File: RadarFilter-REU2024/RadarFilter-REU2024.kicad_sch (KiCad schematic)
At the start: 41 parts, among them J1 Conn_02x15_Odd_Even, J2 Conn_01x04_Pin, J5 Conn_01x04_Pin, J6 Conn_Coaxial, J7 Conn_Coaxial, J8 Conn_Coaxial, J9 Conn_Coaxial, U2 ADA4807-2ARM

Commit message: schematic iteration 1 complete, some project-specific symbols included
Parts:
- removed C6: 0.1uF, Capacitor_SMD:C_0805_2012Metric_Pad1.18x1.45mm_HandSolder, symbol Device:C
- removed J1: Conn_02x15_Odd_Even, Connector_PinSocket_2.54mm:PinSocket_2x15_P2.54mm_Vertical, symbol Connector_Generic:Conn_02x15_Odd_Even
- removed J2 (x2), J5: Conn_01x04_Pin, Connector_PinHeader_2.54mm:PinHeader_1x04_P2.54mm_Horizontal, symbol Connector:Conn_01x04_Pin
- removed J6, J7, J8, J9: Conn_Coaxial, symbol Connector:Conn_Coaxial
- removed R10 (x4), R11 (x4): 10k, Resistor_SMD:R_0805_2012Metric_Pad1.20x1.40mm_HandSolder, symbol Device:R
- removed U2 (x4): ADA4807-2ARM, Package_SO:MSOP-8_3x3mm_P0.65mm, symbol Amplifier_Operational:ADA4807-2ARM
- added C5, C6 (x4): 0.1uF, Capacitor_SMD:C_0805_2012Metric_Pad1.18x1.45mm_HandSolder, symbol Device:C
- added C7: 10uF, Capacitor_SMD:C_0805_2012Metric_Pad1.18x1.45mm_HandSolder, symbol Device:C
- added J1, J2, J3: 73099-0, CONN_73099-0_POM, symbol 73099-0:73099-0
- added U1, U3, U4: 5227161-1, 5227161-1_TYC, symbol 5227161-1:5227161-1
- added U2: ADA4807-2ARM, Package_SO:MSOP-8_3x3mm_P0.65mm, symbol Amplifier_Operational:ADA4807-2ARM
- added unit 1 of U2
- C7: value 0.1uF -> 10uF
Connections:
- net GND: now also C5.2, C6.2, C6.2, C6.2, C6.2, C7.2, J3.1, U1.2, U2.2, U3.2, U4.2
- net V+: now also C6.1, C6.1, J2.1, U2.8 (V+)
- net V-: now also C5.1, C6.1, C6.1, C7.1, J1.1, U2.4 (V-)
- net BNC1I: now reaches R11.2, U2.7
- net BNC1I: now also U1.1
- net BNC2I: now reaches R11.2, U2.7
- net BNC2I: now also U2.1
- net 2+ renamed BNC2Q
- net BNC2Q: now also U4.1
- net BNC2 renamed BNC1Q
- net BNC1Q: now also U3.1
- no-connect marks 18 -> 0
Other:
- note added: "ADP3450 Connection - BNC Female Ports"
- note added: "Power Supply (DPS3340) - Banana Plugs"
- note added: "Trigger"
- note added: "V+/V- Bypass Capacitors"
- note removed: "AD connect"
- note removed: "Channel 3I"
- note removed: "Channel 3Q"
- note removed: "Channel 4I"
- note removed: "Channel 4Q"
- note removed: "Radar 3 Signals"
- note removed: "Radar 4 Signals"
- moved on the sheet: C5, C7, R10, R11, U2B, U2C

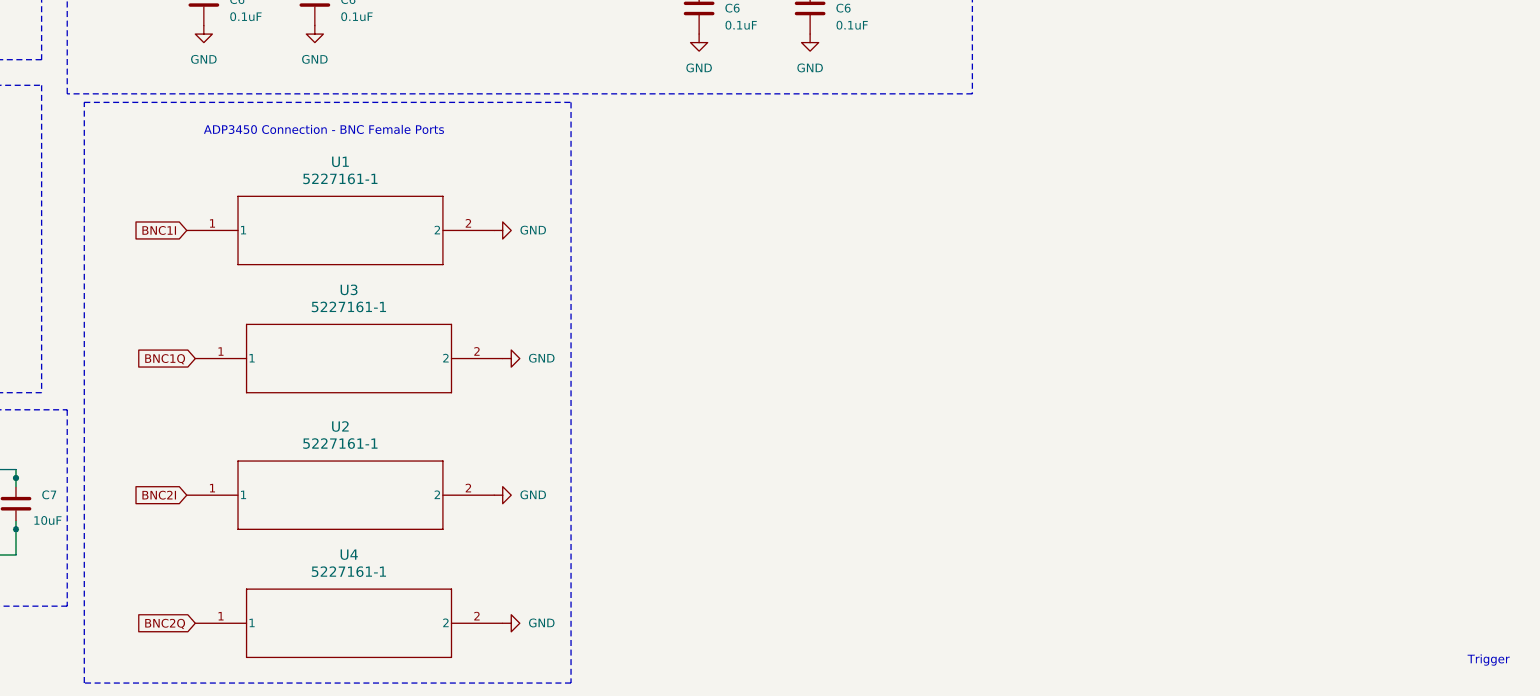
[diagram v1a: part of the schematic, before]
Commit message: changed bnc to sma connectors, attempted start at pcb layout
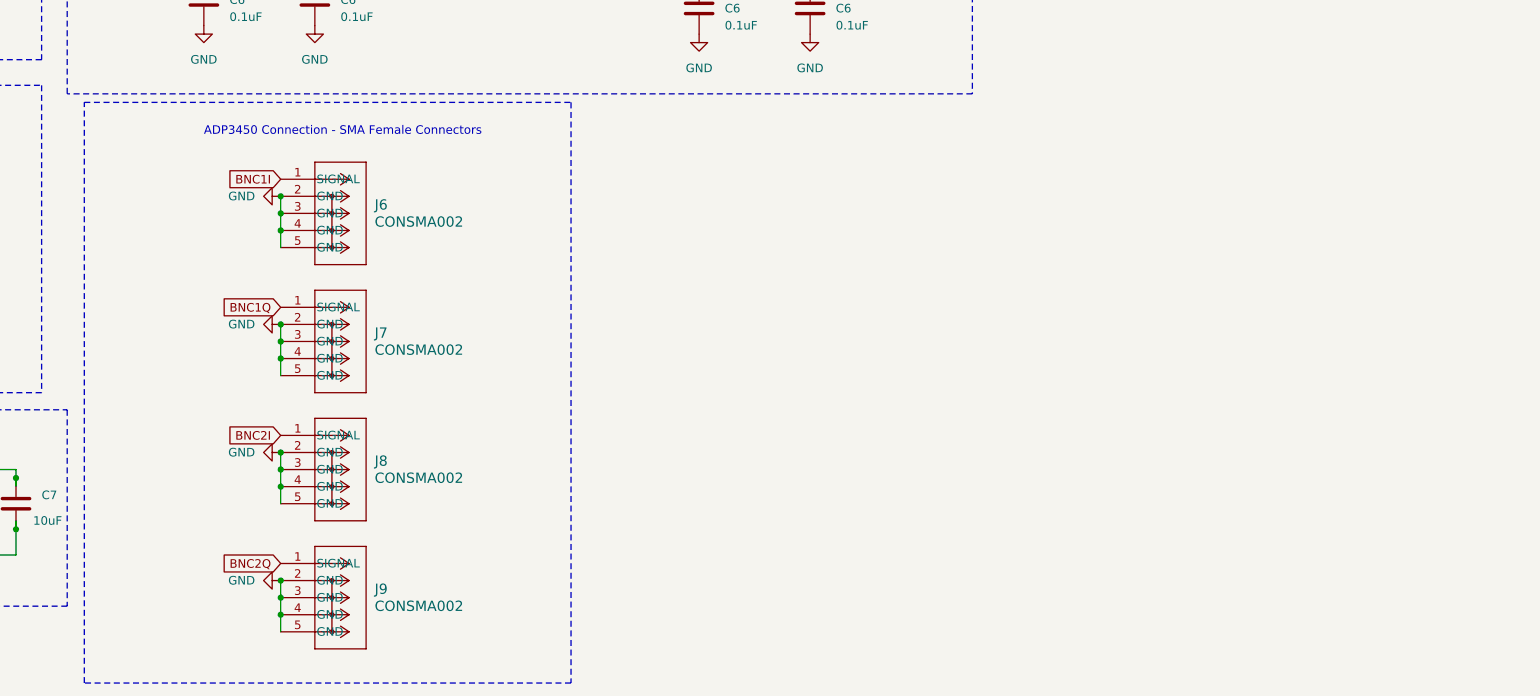
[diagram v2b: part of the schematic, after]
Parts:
- removed U1, U3, U4: 5227161-1, 5227161-1_TYC, symbol 5227161-1:5227161-1
- removed unit 1 of U2
- added J6, J7, J8, J9: CONSMA002, CONSMA002:COAX4_CONSMA002_TEC, symbol CONSMA002:CONSMA002
- J1, J2, J3: footprint CONN_73099-0_POM -> 73099:CONN_73099-0_POM
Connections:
- net BNC1I: now also J6.1 (SIGNAL)
- net BNC1Q: now also J7.1 (SIGNAL)
- net BNC2I: now also J8.1 (SIGNAL)
- net BNC2Q: now also J9.1 (SIGNAL)
- net GND: now also J6.2 (GND), J6.3 (GND), J6.4 (GND), J6.5 (GND), J7.2 (GND), J7.3 (GND), J7.4 (GND), J7.5 (GND), J8.2 (GND), J8.3 (GND), J8.4 (GND), J8.5 (GND), J9.2 (GND), J9.3 (GND), J9.4 (GND), J9.5 (GND)
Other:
- note added: "ADP3450 Connection - SMA Female Connectors"
- note removed: "ADP3450 Connection - BNC Female Ports"
- note removed: "Trigger"

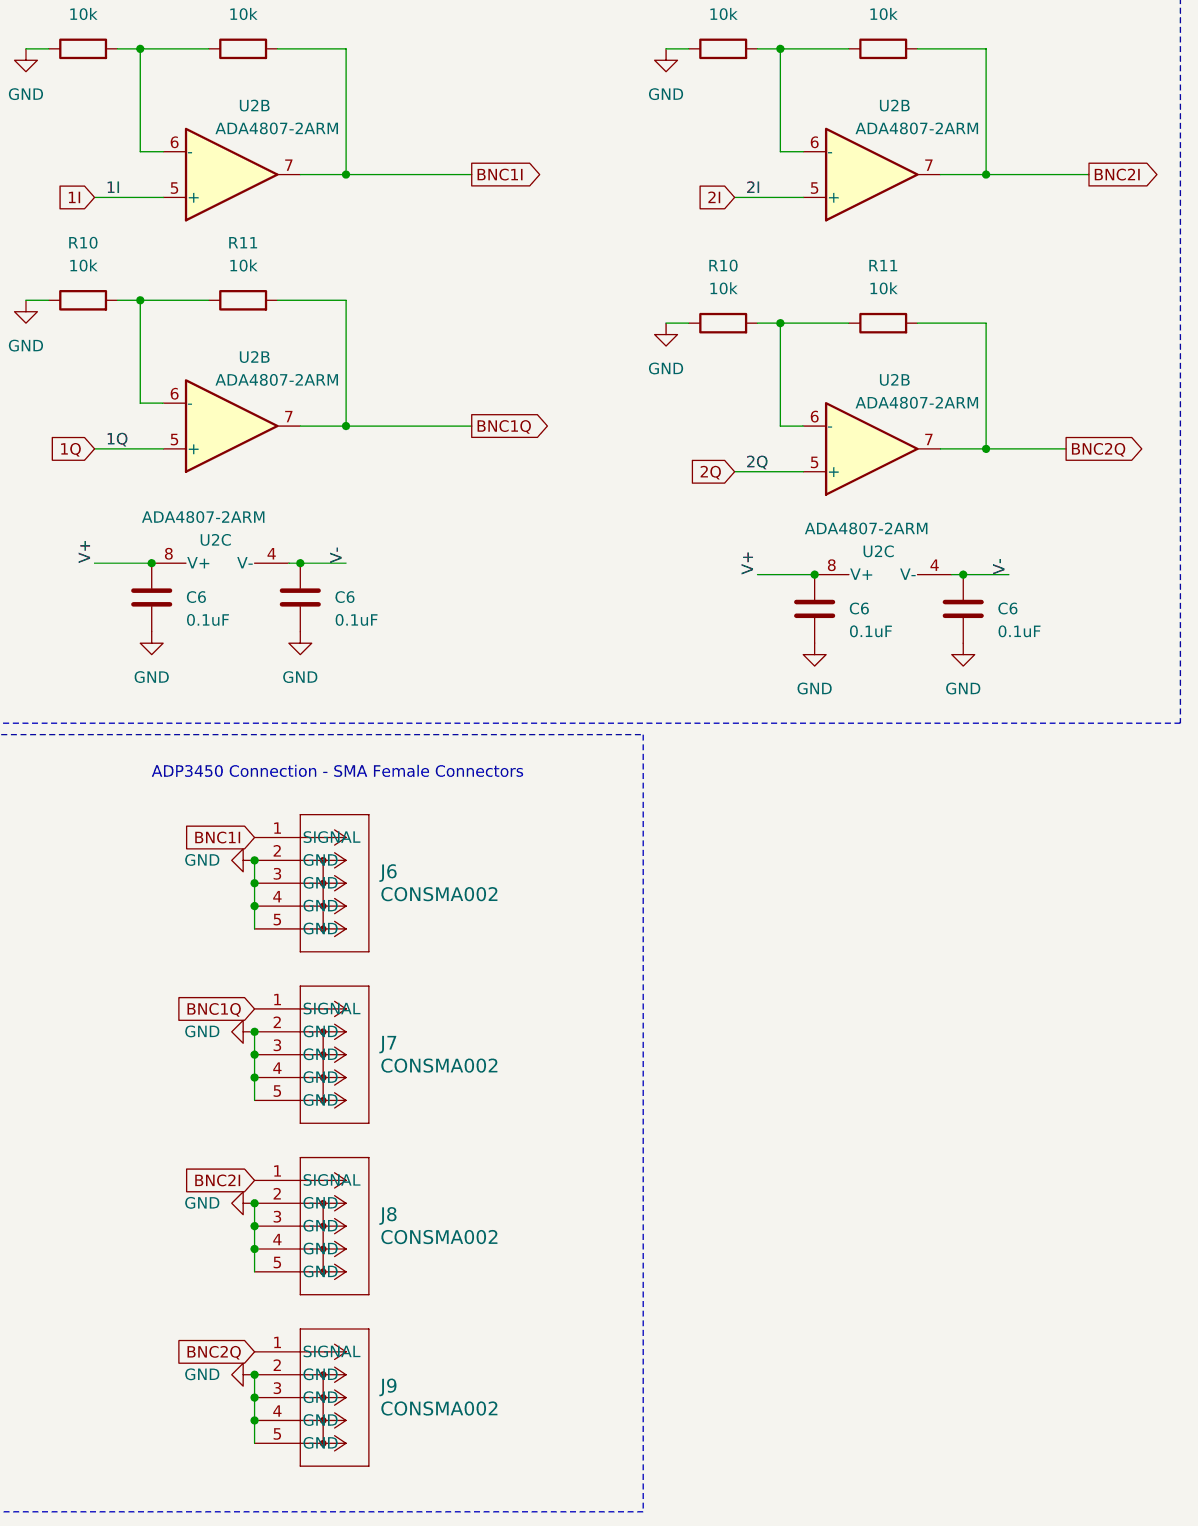
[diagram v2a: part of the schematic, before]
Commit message: changed sma connector footprint, added ground pour to pcb layout
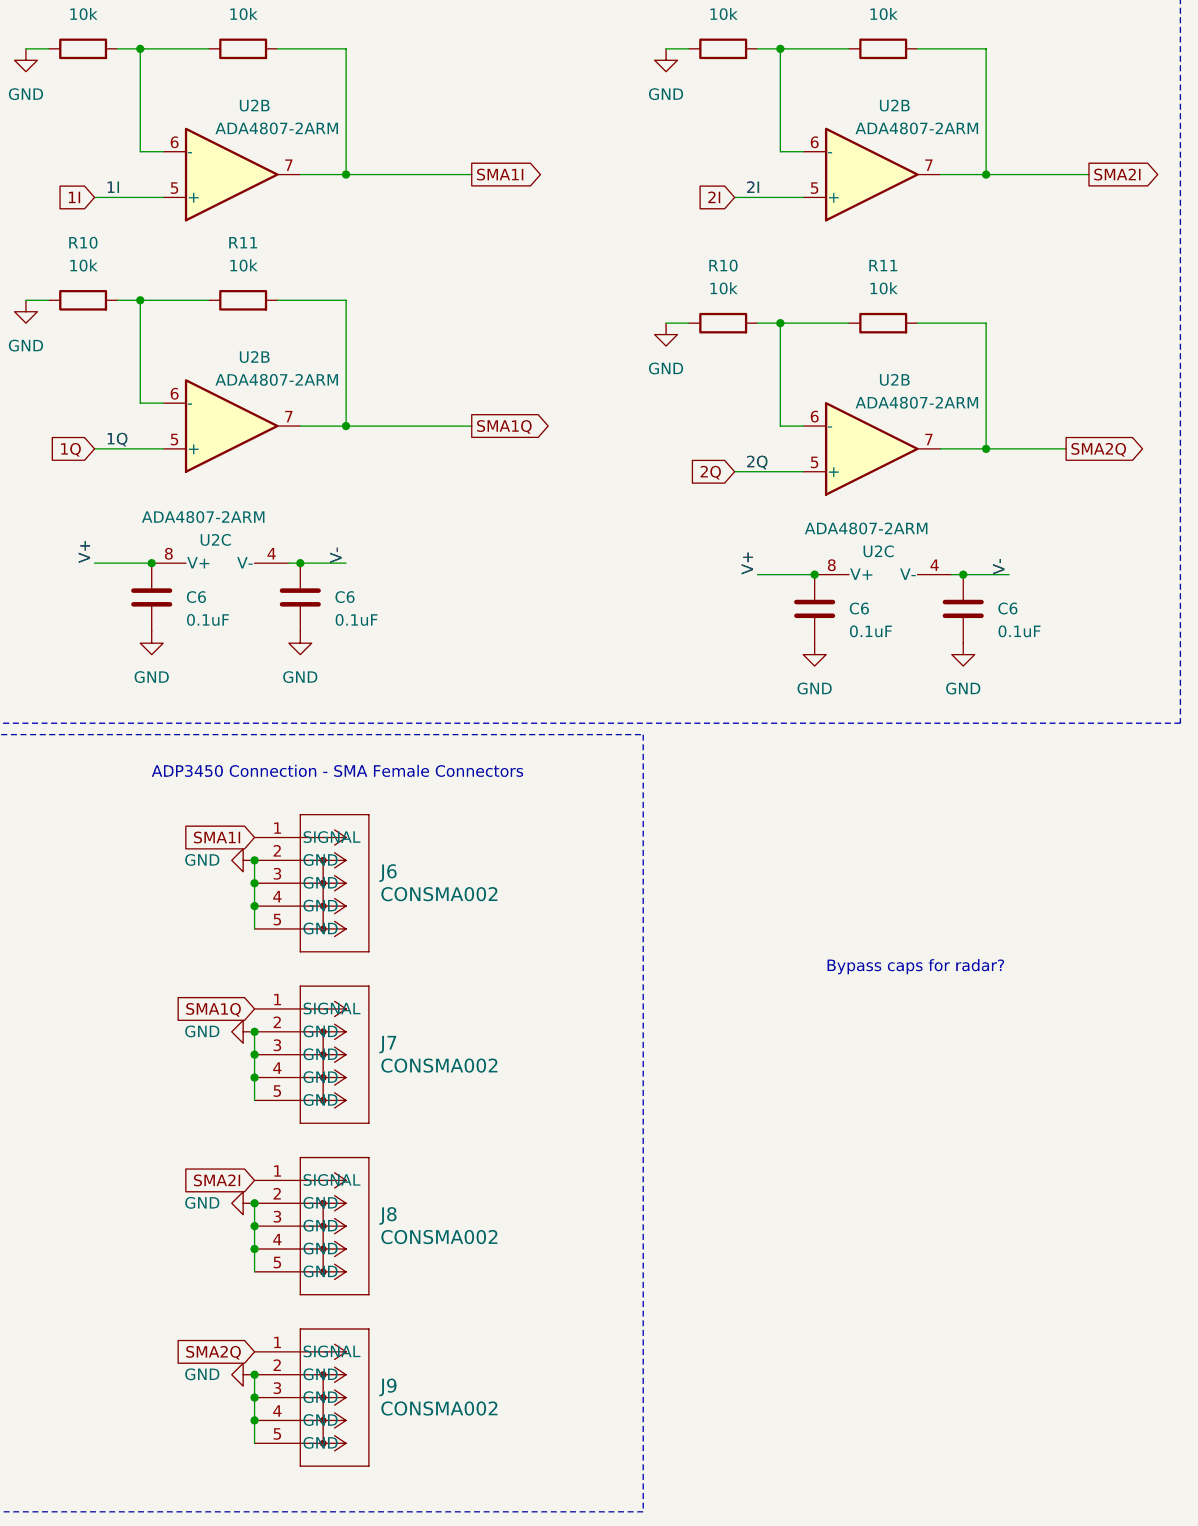
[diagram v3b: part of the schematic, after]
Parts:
- J6, J7, J8, J9: footprint CONSMA002:COAX4_CONSMA002_TEC -> 0731000115:COAX4GND_731000115_MOL
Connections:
- net BNC1I renamed SMA1I
- net BNC1Q renamed SMA1Q
- net BNC2I renamed SMA2I
- net BNC2Q renamed SMA2Q
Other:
- note added: "Bypass caps for radar?"
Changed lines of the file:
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@@
+    (effects (font (size 1.27 1.27)) (justify left bottom))
+  )
+  (text "Bypass caps for radar?" (at 166.37 140.97 0)
     (effects (font (size 1.27 1.27)) (justify left bottom))
   )
@@
     (effects (font (size 1.27 1.27)) (justify left bottom))
   )
-  (global_label "BNC1I" (shape output) (at 127 52.07 0) (fields_autoplaced)
+  (global_label "SMA1I" (shape output) (at 127 52.07 0) (fields_autoplaced)
     (effects (font (size 1.27 1.27)) (justify left))
-    (property "Intersheetrefs" "${INTERSHEET_REFS}" (at 135.67 52.07 0)
+    (property "Intersheetrefs" "${INTERSHEET_REFS}" (at 135.549 52.07 0)
       (effects (font (size 1.27 1.27)) (justify left) hide)
     )
@@
     )
   )
-  (global_label "BNC2Q" (shape input) (at 102.87 182.88 180) (fields_autoplaced)
+  (global_label "SMA2Q" (shape input) (at 102.87 182.88 180) (fields_autoplaced)
     (effects (font (size 1.27 1.27)) (justify right))
-    (property "Intersheetrefs" "${INTERSHEET_REFS}" (at 93.4743 182.88 0)
+    (property "Intersheetrefs" "${INTERSHEET_REFS}" (at 93.5953 182.88 0)
       (effects (font (size 1.27 1.27)) (justify right) hide)
     )
   )
-  (global_label "BNC1Q" (shape output) (at 127 80.01 0) (fields_autoplaced)
+  (global_label "SMA1Q" (shape output) (at 127 80.01 0) (fields_autoplaced)
     (effects (font (size 1.27 1.27)) (justify left))
-    (property "Intersheetrefs" "${INTERSHEET_REFS}" (at 136.3957 80.01 0)
+    (property "Intersheetrefs" "${INTERSHEET_REFS}" (at 136.2747 80.01 0)
       (effects (font (size 1.27 1.27)) (justify left) hide)
     )
   )
-  (global_label "BNC2I" (shape output) (at 195.58 52.07 0) (fields_autoplaced)
+  (global_label "SMA2I" (shape output) (at 195.58 52.07 0) (fields_autoplaced)
     (effects (font (size 1.27 1.27)) (justify left))
-    (property "Intersheetrefs" "${INTERSHEET_REFS}" (at 204.25 52.07 0)
+    (property "Intersheetrefs" "${INTERSHEET_REFS}" (at 204.129 52.07 0)
       (effects (font (size 1.27 1.27)) (justify left) hide)
     )
@@
     )
   )
-  (global_label "BNC1I" (shape input) (at 102.87 125.73 180) (fields_autoplaced)
+  (global_label "SMA1I" (shape input) (at 102.87 125.73 180) (fields_autoplaced)
     (effects (font (size 1.27 1.27)) (justify right))
-    (property "Intersheetrefs" "${INTERSHEET_REFS}" (at 94.2 125.73 0)
+    (property "Intersheetrefs" "${INTERSHEET_REFS}" (at 94.321 125.73 0)
       (effects (font (size 1.27 1.27)) (justify right) hide)
     )
@@
     )
   )
-  (global_label "BNC2I" (shape input) (at 102.87 163.83 180) (fields_autoplaced)
+  (global_label "SMA2I" (shape input) (at 102.87 163.83 180) (fields_autoplaced)
     (effects (font (size 1.27 1.27)) (justify right))
-    (property "Intersheetrefs" "${INTERSHEET_REFS}" (at 94.2 163.83 0)
+    (property "Intersheetrefs" "${INTERSHEET_REFS}" (at 94.321 163.83 0)
       (effects (font (size 1.27 1.27)) (justify right) hide)
     )
@@
     )
   )
-  (global_label "BNC2Q" (shape output) (at 193.04 82.55 0) (fields_autoplaced)
+  (global_label "SMA2Q" (shape output) (at 193.04 82.55 0) (fields_autoplaced)
     (effects (font (size 1.27 1.27)) (justify left))
-    (property "Intersheetrefs" "${INTERSHEET_REFS}" (at 202.4357 82.55 0)
+    (property "Intersheetrefs" "${INTERSHEET_REFS}" (at 202.3147 82.55 0)
       (effects (font (size 1.27 1.27)) (justify left) hide)
     )
   )
-  (global_label "BNC1Q" (shape input) (at 102.87 144.78 180) (fields_autoplaced)
+  (global_label "SMA1Q" (shape input) (at 102.87 144.78 180) (fields_autoplaced)
     (effects (font (size 1.27 1.27)) (justify right))
-    (property "Intersheetrefs" "${INTERSHEET_REFS}" (at 93.4743 144.78 0)
+    (property "Intersheetrefs" "${INTERSHEET_REFS}" (at 93.5953 144.78 0)
       (effects (font (size 1.27 1.27)) (justify right) hide)
     )
@@
       (effects (font (size 1.524 1.524)) (justify left))
     )
-    (property "Footprint" "CONSMA002:COAX4_CONSMA002_TEC" (at 102.87 144.78 0)
+    (property "Footprint" "0731000115:COAX4GND_731000115_MOL" (at 102.87 144.78 0)
       (effects (font (size 1.27 1.27) italic) hide)
     )
@@
       (effects (font (size 1.524 1.524)) (justify left))
     )
-    (property "Footprint" "CONSMA002:COAX4_CONSMA002_TEC" (at 102.87 125.73 0)
+    (property "Footprint" "0731000115:COAX4GND_731000115_MOL" (at 102.87 125.73 0)
       (effects (font (size 1.27 1.27) italic) hide)
     )
@@
       (effects (font (size 1.524 1.524)) (justify left))
     )
-    (property "Footprint" "CONSMA002:COAX4_CONSMA002_TEC" (at 102.87 182.88 0)
+    (property "Footprint" "0731000115:COAX4GND_731000115_MOL" (at 102.87 182.88 0)
       (effects (font (size 1.27 1.27) italic) hide)
     )
@@
       (effects (font (size 1.524 1.524)) (justify left))
     )
-    (property "Footprint" "CONSMA002:COAX4_CONSMA002_TEC" (at 102.87 163.83 0)
+    (property "Footprint" "0731000115:COAX4GND_731000115_MOL" (at 102.87 163.83 0)
       (effects (font (size 1.27 1.27) italic) hide)
     )
